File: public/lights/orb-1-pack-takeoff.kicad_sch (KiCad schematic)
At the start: 6 parts

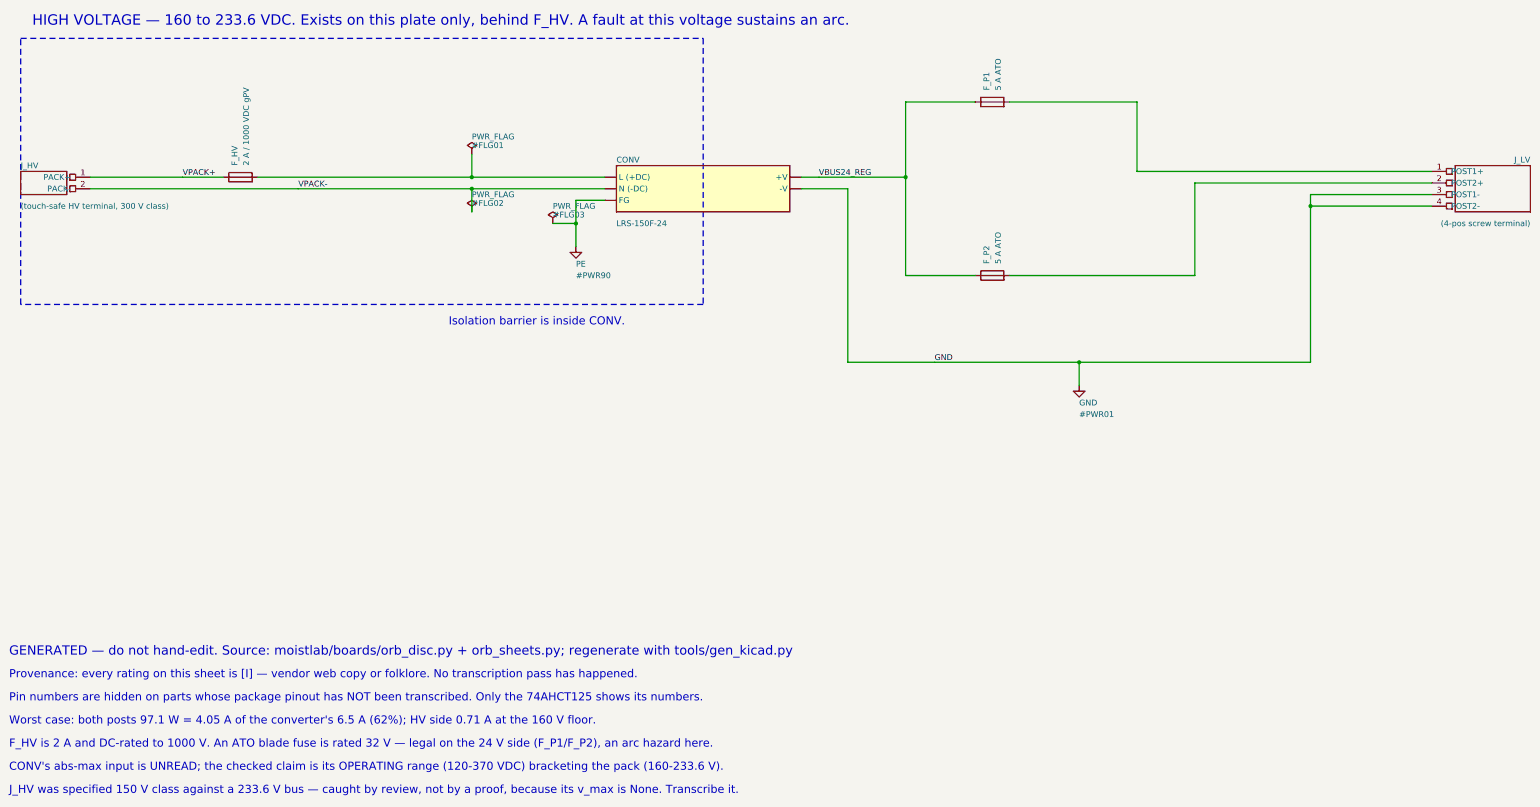
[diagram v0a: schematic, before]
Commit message: solar: h1 solar, OPT4048 sensor, drafted CAD drawings, plain-language sync note
Co-Authored-By: Claude Fable 5 <noreply@anthropic.com>
Claude-Session: https://claude.ai/code/session_01KGs7HAmqeyDzRmkLXBVjfP
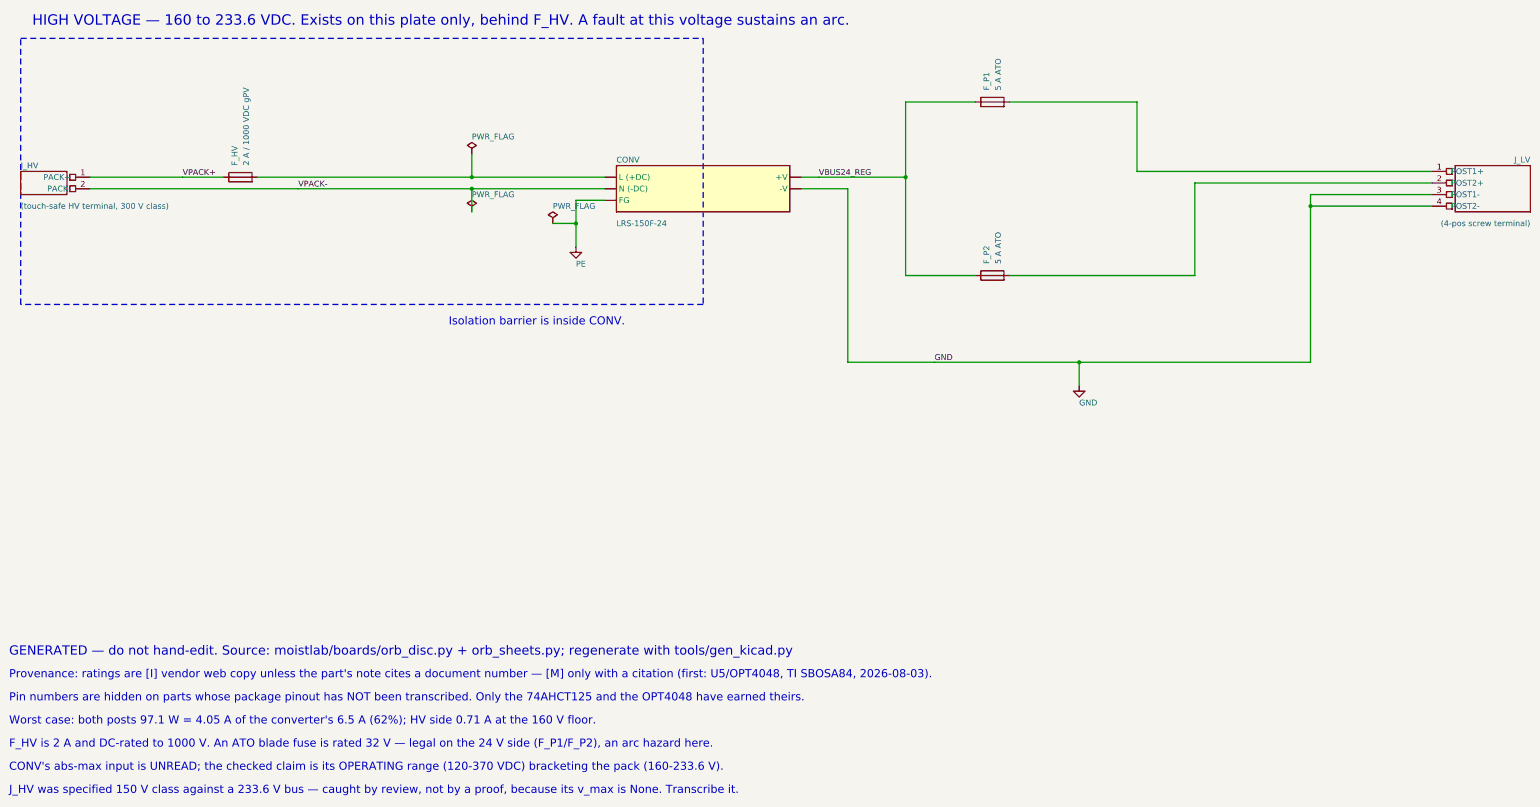
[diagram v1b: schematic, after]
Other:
- note added: "Pin numbers are hidden on parts whose package pinout has NOT been transcribed. Only the 74AHCT125 and the OPT4048 have earned theirs."
- note added: "Provenance: ratings are [I] vendor web copy unless the part's note cites a document number — [M] only with a citation (first: U5/OPT4048, TI SBOSA84, 2026-08-03)."
- note removed: "Pin numbers are hidden on parts whose package pinout has NOT been transcribed. Only the 74AHCT125 shows its numbers."
- note removed: "Provenance: every rating on this sheet is [I] — vendor web copy or folklore. No transcription pass has happened."
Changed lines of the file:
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@@
 	(text "Isolation barrier is inside CONV." (exclude_from_sim no) (at 121.92 118.11 0) (effects (font (size 1.778 1.778)) (justify left)))
 	(text "GENERATED — do not hand-edit. Source: moistlab/boards/orb_disc.py + orb_sheets.py; regenerate with tools/gen_kicad.py" (exclude_from_sim no) (at 25.4 190.5 0) (effects (font (size 2.032 2.032)) (justify left)))
-	(text "Provenance: every rating on this sheet is [I] — vendor web copy or folklore. No transcription pass has happened." (exclude_from_sim no) (at 25.4 195.58 0) (effects (font (size 1.778 1.778)) (justify left)))
-	(text "Pin numbers are hidden on parts whose package pinout has NOT been transcribed. Only the 74AHCT125 shows its numbers." (exclude_from_sim no) (at 25.4 200.66 0) (effects (font (size 1.778 1.778)) (justify left)))
+	(text "Provenance: ratings are [I] vendor web copy unless the part's note cites a document number — [M] only with a citation (first: U5/OPT4048, TI SBOSA84, 2026-08-03)." (exclude_from_sim no) (at 25.4 195.58 0) (effects (font (size 1.778 1.778)) (justify left)))
+	(text "Pin numbers are hidden on parts whose package pinout has NOT been transcribed. Only the 74AHCT125 and the OPT4048 have earned theirs." (exclude_from_sim no) (at 25.4 200.66 0) (effects (font (size 1.778 1.778)) (justify left)))
 	(text "Worst case: both posts 97.1 W = 4.05 A of the converter's 6.5 A (62%); HV side 0.71 A at the 160 V floor." (exclude_from_sim no) (at 25.4 205.74 0) (effects (font (size 1.778 1.778)) (justify left)))
 	(text "F_HV is 2 A and DC-rated to 1000 V. An ATO blade fuse is rated 32 V — legal on the 24 V side (F_P1/F_P2), an arc hazard here." (exclude_from_sim no) (at 25.4 210.82 0) (effects (font (size 1.778 1.778)) (justify left)))
@@
 	(symbol (lib_id "moistlab:PWR_FLAG") (at 127 81.28 0) (unit 1)
 		(exclude_from_sim no) (in_bom yes) (on_board yes) (dnp no)
-		(property "Reference" "#FLG01" (at 127 79.375 0) (effects (font (size 1.27 1.27)) (justify left)))
+		(property "Reference" "#FLG01" (at 127 79.375 0) (effects (font (size 1.27 1.27)) (justify left) (hide yes)))
 		(property "Value" "PWR_FLAG" (at 127 77.47 0) (effects (font (size 1.27 1.27)) (justify left)))
 		(property "Footprint" "" (at 127 81.28 0) (effects (font (size 1.27 1.27)) (hide yes)))
@@
 	(symbol (lib_id "moistlab:PWR_FLAG") (at 127 93.98 0) (unit 1)
 		(exclude_from_sim no) (in_bom yes) (on_board yes) (dnp no)
-		(property "Reference" "#FLG02" (at 127 92.075 0) (effects (font (size 1.27 1.27)) (justify left)))
+		(property "Reference" "#FLG02" (at 127 92.075 0) (effects (font (size 1.27 1.27)) (justify left) (hide yes)))
 		(property "Value" "PWR_FLAG" (at 127 90.17 0) (effects (font (size 1.27 1.27)) (justify left)))
 		(property "Footprint" "" (at 127 93.98 0) (effects (font (size 1.27 1.27)) (hide yes)))
@@
 	(symbol (lib_id "moistlab:PE") (at 149.86 101.6 0) (unit 1)
 		(exclude_from_sim no) (in_bom yes) (on_board yes) (dnp no)
-		(property "Reference" "#PWR90" (at 149.86 107.95 0) (effects (font (size 1.27 1.27)) (justify left)))
+		(property "Reference" "#PWR90" (at 149.86 107.95 0) (effects (font (size 1.27 1.27)) (justify left) (hide yes)))
 		(property "Value" "PE" (at 149.86 105.41 0) (effects (font (size 1.27 1.27)) (justify left)))
 		(property "Footprint" "" (at 149.86 101.6 0) (effects (font (size 1.27 1.27)) (hide yes)))
@@
 	(symbol (lib_id "moistlab:PWR_FLAG") (at 144.78 96.52 0) (unit 1)
 		(exclude_from_sim no) (in_bom yes) (on_board yes) (dnp no)
-		(property "Reference" "#FLG03" (at 144.78 94.615 0) (effects (font (size 1.27 1.27)) (justify left)))
+		(property "Reference" "#FLG03" (at 144.78 94.615 0) (effects (font (size 1.27 1.27)) (justify left) (hide yes)))
 		(property "Value" "PWR_FLAG" (at 144.78 92.71 0) (effects (font (size 1.27 1.27)) (justify left)))
 		(property "Footprint" "" (at 144.78 96.52 0) (effects (font (size 1.27 1.27)) (hide yes)))
@@
 	(symbol (lib_id "moistlab:GND") (at 260.35 132.08 0) (unit 1)
 		(exclude_from_sim no) (in_bom yes) (on_board yes) (dnp no)
-		(property "Reference" "#PWR01" (at 260.35 138.43 0) (effects (font (size 1.27 1.27)) (justify left)))
+		(property "Reference" "#PWR01" (at 260.35 138.43 0) (effects (font (size 1.27 1.27)) (justify left) (hide yes)))
 		(property "Value" "GND" (at 260.35 135.89 0) (effects (font (size 1.27 1.27)) (justify left)))
 		(property "Footprint" "" (at 260.35 132.08 0) (effects (font (size 1.27 1.27)) (hide yes)))
